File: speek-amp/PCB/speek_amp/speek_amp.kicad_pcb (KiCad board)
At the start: 2 copper layers, 70 parts, among them J1 Conn_01x02, J2 R_Tweeter, J3 R_Woofer, J5 L_Tweeter, J6 L_Sub, J7 L_Woofer, U1 TPA3116D2DAD_C2865736, U2 10uH, U3 10uH, U4 XT60, U5 10uH, U6 10uH, U7 PDMTAT068125-151MLU, U8 PDMTAT068125-151MLU

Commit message: a
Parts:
- added U9: 25PX4700MEFC16X25, easyeda2kicad:CAP-TH_BD16.0-P7.50-D1.2-FD, F.Cu at (22.1, 84.3)
- moved C1 143.4 mm to (45.7, 21.7)
- moved C10 143.4 mm to (45.7, 30.3)
- moved C11 143.4 mm to (45.7, 32.5)
- moved C12 143.4 mm to (45.7, 34.6)
- moved C21 143.4 mm to (51.5, 21.7)
- moved C22 143.4 mm to (51.5, 23.9)
- moved C23 143.4 mm to (51.5, 26.0)
- moved C24 143.4 mm to (51.5, 28.2)
- moved C25 143.4 mm to (51.5, 30.3)
- moved C26 143.4 mm to (51.5, 32.5)
- moved C27 143.4 mm to (51.5, 34.6)
- moved C6 143.4 mm to (45.7, 23.9)
- moved C7 143.4 mm to (45.7, 26.0)
- moved C8 143.4 mm to (45.7, 28.2)
- moved J1 143.4 mm to (59.2, 25.4)
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
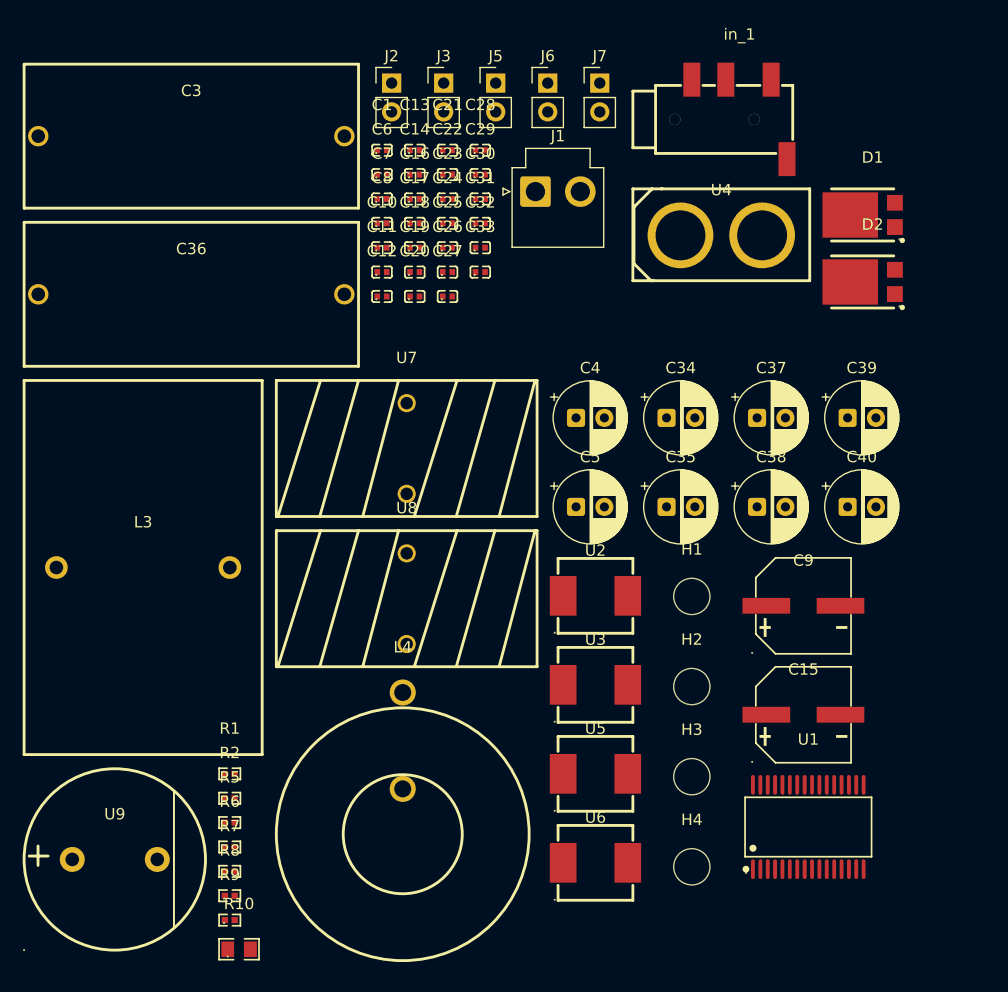
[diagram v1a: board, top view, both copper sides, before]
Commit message: [Speek Amp] Schematic rework
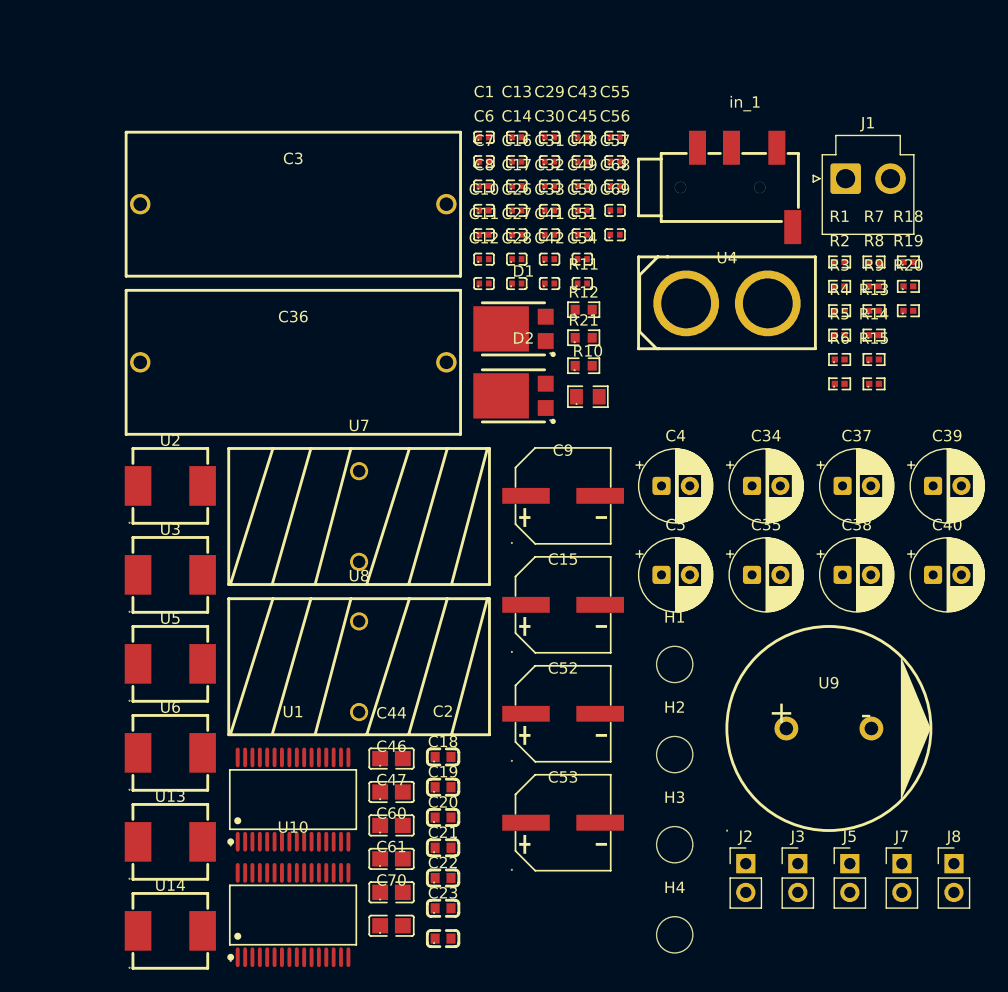
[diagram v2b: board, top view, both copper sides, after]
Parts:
- removed C24, C25: 100nF, easyeda2kicad:C0402
- removed J6: L_Sub, Connector_PinHeader_2.54mm:PinHeader_1x02_P2.54mm_Vertical
- removed L3: 1mH, easyeda2kicad:IND-TH_L33.0-W21.0-P15.3-D1.0
- removed L4: 220 uH, easyeda2kicad:IND-TH_BD22.3-P8.50-D1.2_XR068125TS221MHL8
- added C2: 100nF, easyeda2kicad:C0603, F.Cu at (51.1, 75.2)
- added C41: 1uF, easyeda2kicad:C0402, F.Cu at (60.5, 31.3)
- added C42: 1uF, easyeda2kicad:C0402, F.Cu at (60.5, 33.5)
- added C43: 100nF, easyeda2kicad:C0402, F.Cu at (63.4, 20.6)
- added C44: 680nF, easyeda2kicad:C0805, F.Cu at (46.5, 75.4)
- added C45: 1uF, easyeda2kicad:C0402, F.Cu at (63.4, 22.7)
- added C46: 680nF, easyeda2kicad:C0805, F.Cu at (46.5, 78.3)
- added C47: 680nF, easyeda2kicad:C0805, F.Cu at (46.5, 81.3)
- added C48: 220nF, easyeda2kicad:C0402, F.Cu at (63.4, 24.9)
- added C49: 220nF, easyeda2kicad:C0402, F.Cu at (63.4, 27.0)
- added C50: 220nF, easyeda2kicad:C0402, F.Cu at (63.4, 29.2)
- added C51: 220nF, easyeda2kicad:C0402, F.Cu at (63.4, 31.3)
- added C52: 220uF, easyeda2kicad:CAP-SMD_BD8.0-L8.3-W8.3-FD, F.Cu at (61.7, 71.4)
- added C53: 220uF, easyeda2kicad:CAP-SMD_BD8.0-L8.3-W8.3-FD, F.Cu at (61.7, 81.0)
- added C54: 100nF, easyeda2kicad:C0402, F.Cu at (63.4, 33.5)
- added C55: 100nF, easyeda2kicad:C0402, F.Cu at (66.3, 20.6)
- added C56: 1nF, easyeda2kicad:C0402, F.Cu at (66.3, 22.7)
- added C57: 1nF, easyeda2kicad:C0402, F.Cu at (66.3, 24.9)
- added C60: 680nF, easyeda2kicad:C0805, F.Cu at (46.5, 84.2)
- added C61: 680nF, easyeda2kicad:C0805, F.Cu at (46.5, 87.2)
- added C68: 1nF, easyeda2kicad:C0402, F.Cu at (66.3, 27.0)
- added C69: 1nF, easyeda2kicad:C0402, F.Cu at (66.3, 29.2)
- added C70: 680nF, easyeda2kicad:C0805, F.Cu at (46.5, 90.1)
- added J8: L_Sub, Connector_PinHeader_2.54mm:PinHeader_1x02_P2.54mm_Vertical, F.Cu at (96.1, 84.6)
- added R11: 3.2k, easyeda2kicad:R0603, F.Cu at (63.5, 35.8)
- added R12: 47k, easyeda2kicad:R0603, F.Cu at (63.5, 38.3)
- added R13: 3.3, easyeda2kicad:R0402, F.Cu at (89.1, 38.0)
- added R14: 100k, easyeda2kicad:R0402, F.Cu at (89.1, 40.2)
- added R15: 100k, easyeda2kicad:R0402, F.Cu at (89.1, 42.3)
- added R18: 3.3, easyeda2kicad:R0402, F.Cu at (92.1, 31.6)
- added R19: 3.3, easyeda2kicad:R0402, F.Cu at (92.1, 33.7)
- added R20: 10k, easyeda2kicad:R0402, F.Cu at (92.1, 35.9)
- added R21: 75k, easyeda2kicad:R0603, F.Cu at (63.5, 40.7)
- added R3: 10k, easyeda2kicad:R0402, F.Cu at (86.1, 35.9)
- added R4: 10k, easyeda2kicad:R0402, F.Cu at (86.1, 38.0)
- added U10: TPA3116D2DAD_C2865736, easyeda2kicad:HTSSOP-32_L11.0-W6.1-P0.65-LS8.1-BL, F.Cu at (37.9, 89.2)
- added U13: 10uH, easyeda2kicad:IND-SMD_L7.2-W6.6_GPSR07X0, F.Cu at (27.0, 82.7)
- added U14: 10uH, easyeda2kicad:IND-SMD_L7.2-W6.6_GPSR07X0, F.Cu at (27.0, 90.6)
- C18, C19, C20, C21: value 1uF -> 10nF; footprint easyeda2kicad:C0402 -> easyeda2kicad:C0603
- C22, C23: value 100nF -> 10nF; footprint easyeda2kicad:C0402 -> easyeda2kicad:C0603
- U9: value 25PX4700MEFC16X25 -> 50PX4700MEFC18X40; footprint easyeda2kicad:CAP-TH_BD16.0-P7.50-D1.2-FD -> easyeda2kicad:CAP-TH_BD18.0-P7.50-D0.8-FD
- moved R7 78.2 mm to (89.1, 31.6)
- moved R8 78.2 mm to (89.1, 33.7)
- moved R9 78.2 mm to (89.1, 35.9)
- moved J2 75.6 mm to (77.8, 84.6)
- moved J3 75.6 mm to (82.4, 84.6)
- moved J5 75.6 mm to (87.0, 84.6)
- moved J7 73.8 mm to (91.6, 84.6)
- moved R2 70.2 mm to (86.1, 33.7)
- moved R1 70.2 mm to (86.1, 31.6)
- moved R5 67.6 mm to (86.1, 40.2)
- moved R6 67.6 mm to (86.1, 42.3)
- moved C23 65.2 mm to (51.1, 91.3)
- moved C22 64.7 mm to (51.1, 88.6)
- moved C21 64.2 mm to (51.1, 85.9)
- moved U9 64.0 mm to (85.1, 72.7)
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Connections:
- C19 pad 1: /AMP_NR -> GND
- C19 pad 2: GND -> /AMP_NR
- C20 pad 1: /AMP_PL -> GND
- C20 pad 2: GND -> /AMP_PL
- C21 pad 1: /AMP_NL -> GND
- C21 pad 2: GND -> /AMP_NL
- C22 pad 1: /AMP_PR -> /SUB_P
- C23 pad 2: /AMP_NR -> /SUB_N
- U9 pad 1: /VCC -> /_VOUT

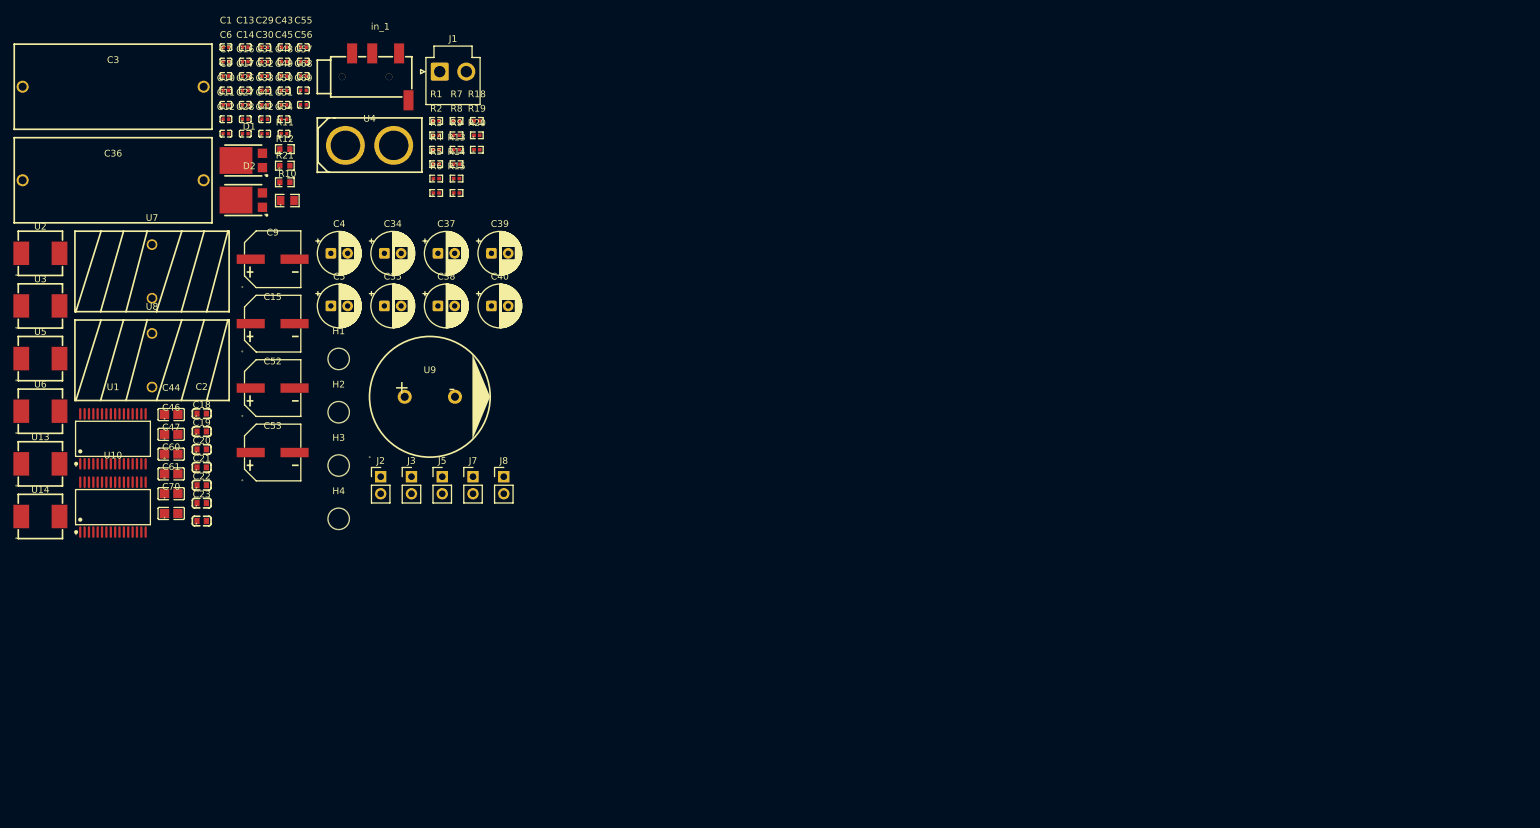
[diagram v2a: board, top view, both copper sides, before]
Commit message: [Speek amp] Prelim placement!!! [0.62 hours]
Long bom, many caps to place...
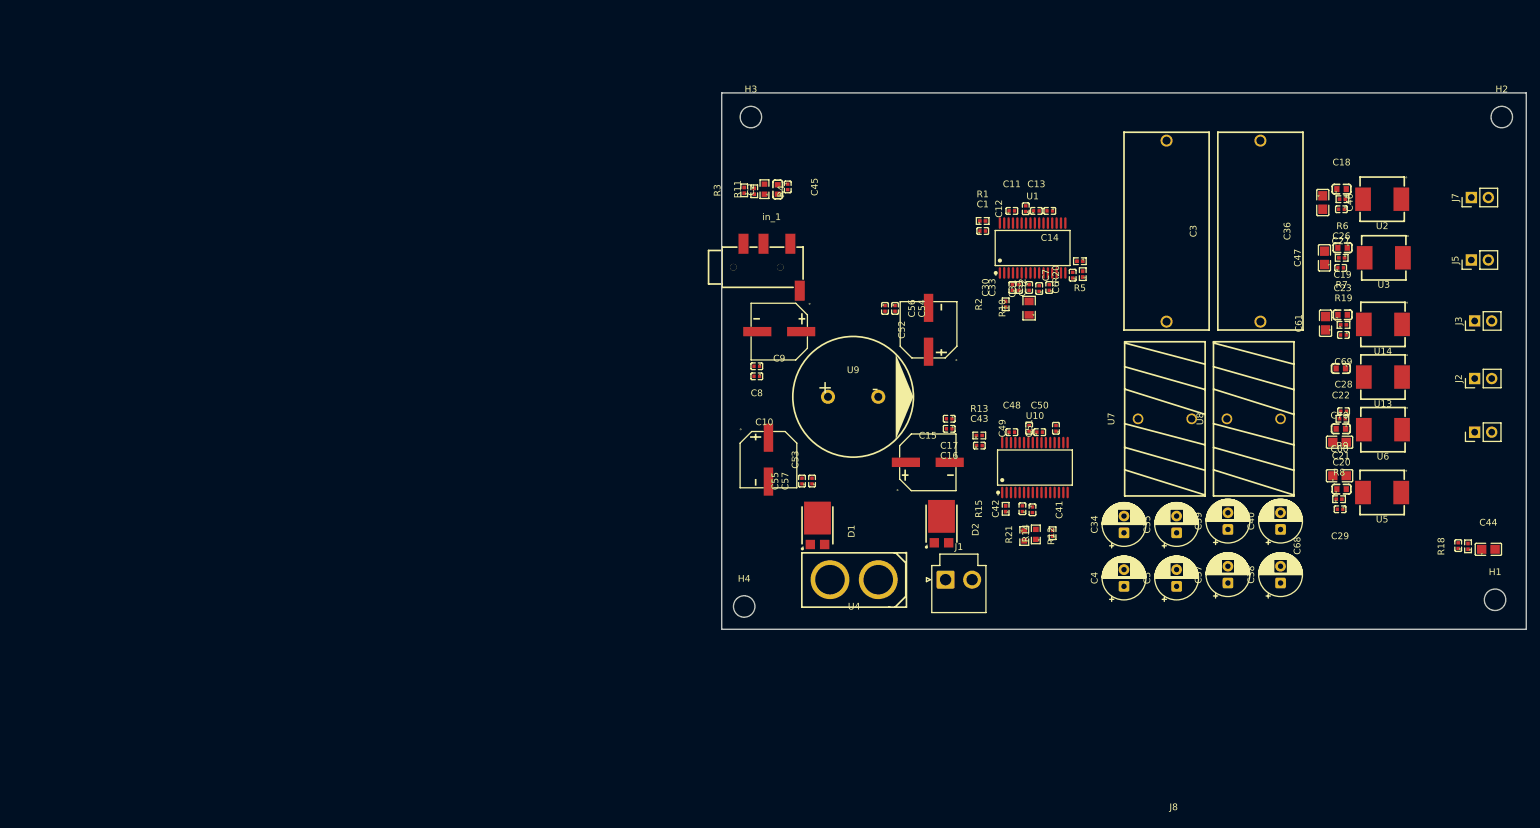
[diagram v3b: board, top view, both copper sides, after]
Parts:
- moved U14 202.3 mm to (227.3, 61.9), turned to 180 degrees
- moved U5 201.1 mm to (227.2, 87.0), turned to 180 degrees
- moved U13 200.7 mm to (227.3, 69.8), turned to 180 degrees
- moved U3 200.5 mm to (227.4, 52.0), turned to 180 degrees
- moved U2 200.3 mm to (227.2, 43.2), turned to 180 degrees
- moved U6 200.3 mm to (227.3, 77.6), turned to 180 degrees
- moved C44 197.5 mm to (243.0, 95.5)
- moved C68 185.1 mm to (238.5, 94.9), turned to 90 degrees
- moved H2 179.0 mm to (245.0, 31.0)
- moved H1 176.2 mm to (244.0, 103.0)
- moved C46 175.2 mm to (218.3, 43.8), turned to -90 degrees
- moved C70 174.6 mm to (220.8, 79.5)
- moved C29 174.6 mm to (220.9, 89.5), turned to 180 degrees
- moved C47 174.5 mm to (218.6, 52.0), turned to 90 degrees
- moved C60 174.3 mm to (220.8, 84.5)
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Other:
- board outline added: 120 x 80 mm

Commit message: [Speek Amp] routing !! [1.25 hours]
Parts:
- moved C38 73.7 mm to (239.0, 31.9), turned to 180 degrees
- moved C29 73.5 mm to (175.0, 32.1), turned to 90 degrees
- moved R8 71.4 mm to (176.5, 31.9), turned to -90 degrees
- moved C37 71.0 mm to (223.0, 32.0), turned to 180 degrees
- moved C20 69.2 mm to (178.0, 32.3), turned to -90 degrees
- moved U5 68.3 mm to (179.0, 38.5), turned to 90 degrees
- moved C60 66.5 mm to (180.0, 32.0), turned to -90 degrees
- moved C40 63.5 mm to (231.0, 31.9), turned to 180 degrees
- moved C39 62.3 mm to (236.0, 39.0), turned to 180 degrees
- moved U2 61.2 mm to (166.2, 37.8), turned to 90 degrees
- moved R6 53.4 mm to (169.0, 32.1), turned to -90 degrees
- moved C26 52.1 mm to (170.5, 32.2), turned to -90 degrees
- moved C46 51.1 mm to (169.2, 29.5), turned to 180 degrees
- moved C18 50.0 mm to (172.0, 32.3), turned to -90 degrees
- moved C4 46.9 mm to (233.5, 87.3), turned to 180 degrees
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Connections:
- U9 pad 1: /_VOUT -> /VCC
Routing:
- net /VCC: track 0.00 -> 233.7 mm
- net /OUTNR: track 0.00 -> 105.8 mm
- net /_OUTP: track 0.00 -> 97.1 mm, vias 0 -> 15
- net /_OUTN: track 0.00 -> 87.1 mm
- net /AMP_PR: track 0.00 -> 85.5 mm
- net /AMP_PL: track 0.00 -> 85.4 mm, vias 0 -> 6
- net /INL: track 0.00 -> 71.5 mm, vias 0 -> 2
- net Net-(U10-RINP): track 0.00 -> 71.4 mm, vias 0 -> 2
- net /INR: track 0.00 -> 65.1 mm, vias 0 -> 2
- net /OUTNL: track 0.00 -> 63.0 mm
- net Net-(C34-Pad1): track 0.00 -> 62.6 mm
- net GND: track 0.00 -> 60.9 mm, vias 0 -> 38
- net Net-(J3-Pin_1): track 0.00 -> 56.5 mm
- net /SYNC: track 0.00 -> 50.2 mm, vias 0 -> 2
- net Net-(J2-Pin_1): track 0.00 -> 49.5 mm
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- added copper zone on B.Cu, net GND
- added copper zone on F.Cu, net GND

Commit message: e
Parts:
- removed J1: Conn_01x02, Connector_JST:JST_VH_B2P-VH-B_1x02_P3.96mm_Vertical
- removed J2: R_Tweeter, Connector_PinHeader_2.54mm:PinHeader_1x02_P2.54mm_Vertical
- removed J3: R_Woofer, Connector_PinHeader_2.54mm:PinHeader_1x02_P2.54mm_Vertical
- removed J5: L_Tweeter, Connector_PinHeader_2.54mm:PinHeader_1x02_P2.54mm_Vertical
- removed J7: L_Woofer, Connector_PinHeader_2.54mm:PinHeader_1x02_P2.54mm_Vertical
- removed J8: L_Sub, Connector_PinHeader_2.54mm:PinHeader_1x02_P2.54mm_Vertical
- added U11: R_Tweeter, easyeda2kicad:CONN-TH_DB301V-3.5-2P-GN, F.Cu at (244.5, 70.0)
- added U12: R_Woofer, easyeda2kicad:CONN-TH_DB301V-3.5-2P-GN, F.Cu at (244.5, 60.5)
- added U15: L_Tweeter, easyeda2kicad:CONN-TH_DB301V-3.5-2P-GN, F.Cu at (244.5, 51.0)
- added U16: L_Woofer, easyeda2kicad:CONN-TH_DB301V-3.5-2P-GN, F.Cu at (244.5, 41.5)
- added U17: L_Sub, easyeda2kicad:CONN-TH_DB301V-3.5-2P-GN, F.Cu at (244.5, 79.8)
- added U18: J1, easyeda2kicad:CONN-TH_DB301V-3.5-2P-GN, F.Cu at (164.2, 100.1)
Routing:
- net Net-(C37-Pad2): track 35.4 -> 49.3 mm
- net Net-(C36-Pad2): track 37.0 -> 42.0 mm
- net /OUTNR: track 105.8 -> 110.8 mm
- net Net-(C3-Pad2): track 49.5 -> 53.7 mm
- net /AMP_NL: track 38.6 -> 42.6 mm
- net /SUB_P: track 29.9 -> 32.8 mm
- net /AMP_NR: track 41.9 -> 44.7 mm
- net Net-(C34-Pad2): track 56.5 -> 54.5 mm
- net /VCC: track 233.7 -> 233.2 mm

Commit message: vias
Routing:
- net GND: vias 38 -> 268

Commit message: yes!
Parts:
- moved H4 1.41 mm to (133.0, 103.0)
- moved C38 1.00 mm to (238.0, 32.0)
- moved H2 1.00 mm to (244.0, 31.0)
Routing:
- net Net-(C37-Pad2): track 49.3 -> 46.2 mm
- net Net-(C37-Pad1): track 41.7 -> 41.1 mm
- net (no net): vias 0 -> 1
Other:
- board text added: "Speek Amp"
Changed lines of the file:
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@@
 			(layer "F.Mask"
 				(type "Top Solder Mask")
+				(color "Black")
 				(thickness 0.01)
 			)
@@
 			(layer "B.Mask"
 				(type "Bottom Solder Mask")
+				(color "Black")
 				(thickness 0.01)
 			)
@@
 		(capping no)
 		(filling no)
+		(zone_defaults)
 		(pcbplotparams
 			(layerselection 0x00000000_00000000_55555555_5755f5ff)
@@
 	(footprint "Capacitor_THT:CP_Radial_D6.3mm_P2.50mm"
 		(layer "F.Cu")
-		(at 239 31.9 180)
+		(at 238 32 180)
 		(descr "CP, Radial series, Radial, pin pitch=2.50mm, diameter=6.3mm, height=7mm, Electrolytic Capacitor")
 		(tags "CP Radial series Radial pin pitch 2.50mm diameter 6.3mm height 7mm Electrolytic Capacitor")
@@
 	(footprint "MountingHole:MountingHole_3.2mm_M3"
 		(layer "F.Cu")
-		(at 245 31)
+		(at 244 31)
 		(descr "Mounting Hole 3.2mm, M3, no annular, generated by kicad-footprint-generator mountinghole.py")
 		(tags "mountinghole M3")
@@
 	(footprint "MountingHole:MountingHole_3.2mm_M3"
 		(layer "F.Cu")
-		(at 132 104)
+		(at 133 103)
 		(descr "Mounting Hole 3.2mm, M3, no annular, generated by kicad-footprint-generator mountinghole.py")
 		(tags "mountinghole M3")
@@
 		(layer "Edge.Cuts")
 	)
+	(gr_text "Speek Amp"
+		(at 182 101 0)
+		(layer "F.SilkS")
+		(effects
+			(font
+				(size 6 6)
+				(thickness 1)
+				(bold yes)
+			)
+			(justify left bottom)
+		)
+	)
+	(via
+		(at 94 52)
+		(size 0.6)
+		(drill 0.3)
+		(layers "F.Cu" "B.Cu")
+		(net "")
+	)
 	(segment
 		(start 219.675 43.75)
@@
 	)
 	(segment
-		(start 239 36)
-		(end 236 39)
+		(start 238 32)
+		(end 236.4 30.4)
 		(width 1)
 		(layer "B.Cu")
@@
 	)
 	(segment
+		(start 238 32)
+		(end 239 33)
+		(width 1)
+		(layer "B.Cu")
+		(net "Net-(C37-Pad1)")
+	)
+	(segment
 		(start 224.4 33.4)
 		(end 223.6 33.4)
@@
 	)
 	(segment
-		(start 232.514759 30.4)
-		(end 237.5 30.4)
+		(start 223.6 33.4)
+		(end 215 42)
 		(width 1)
 		(layer "B.Cu")
@@
 	)
 	(segment
-		(start 223.6 33.4)
-		(end 215 42)
+		(start 239 33)
+		(end 239 36)
 		(width 1)
 		(layer "B.Cu")
@@
 	)
 	(segment
-		(start 215 42)
-		(end 215 44)
+		(start 232.514759 30.4)
+		(end 236.4 30.4)
 		(width 1)
 		(layer "B.Cu")
@@
 	)
 	(segment
-		(start 239 31.9)
-		(end 239 36)
+		(start 239 36)
+		(end 236 39)
 		(width 1)
 		(layer "B.Cu")
@@
 	)
 	(segment
-		(start 237.5 30.4)
-		(end 239 31.9)
+		(start 215 42)
+		(end 215 44)
 		(width 1)
 		(layer "B.Cu")
@@
 	)
 	(segment
-		(start 230.014759 30.4)
-		(end 235 30.4)
+		(start 228.514759 31.9)
+		(end 230.014759 30.4)
 		(width 1)
 		(layer "F.Cu")
@@
 	)
 	(segment
-		(start 228.514759 31.9)
-		(end 230.014759 30.4)
+		(start 233.9 30.4)
+		(end 235.5 32)
 		(width 1)
 		(layer "F.Cu")
@@
 	)
 	(segment
-		(start 235 30.4)
-		(end 236.5 31.9)
+		(start 230.014759 30.4)
+		(end 233.9 30.4)
 		(width 1)
 		(layer "F.Cu")
@@
 	)
 	(segment
-		(start 233.5 39)
-		(end 237.5 43)
+		(start 235.5 32)
+		(end 236.5 33)
 		(width 1)
 		(layer "B.Cu")
@@
 	)
 	(segment
-		(start 236.5 31.9)
-		(end 236.5 36)
+		(start 241.086253 41)
+		(end 235.5 41)
 		(width 1)
 		(layer "B.Cu")
@@
 	)
 	(segment
-		(start 237.5 43)
-		(end 240.46 43)
+		(start 236.5 33)
+		(end 236.5 36)
 		(width 1)
 		(layer "B.Cu")
@@
 	)
 	(segment
-		(start 246.5 39.586253)
-		(end 246.5 41.25)
+		(start 233.5 39)
+		(end 235.5 41)
 		(width 1)
 		(layer "B.Cu")
@@
 	)
 	(segment
-		(start 246.5 41.25)
-		(end 244.5 43.25)
+		(start 246.5 39.586253)
+		(end 246.5 41.25)
 		(width 1)
 		(layer "B.Cu")
@@
 	)
 	(segment
-		(start 245.133747 38.22)
-		(end 246.5 39.586253)
+		(start 246.5 41.25)
+		(end 244.5 43.25)
 		(width 1)
 		(layer "B.Cu")
@@
 	)
 	(segment
-		(start 240.46 43)
-		(end 240.46 41.626253)
+		(start 236.5 36)
+		(end 233.5 39)
 		(width 1)
 		(layer "B.Cu")
@@
 	)
 	(segment
-		(start 222 30.5)
-		(end 220.5 32)
+		(start 243.866253 38.22)
+		(end 241.086253 41)
 		(width 1)
 		(layer "B.Cu")
@@
 	)
 	(segment
-		(start 236.5 36)
-		(end 233.5 39)
+		(start 245.133747 38.22)
+		(end 246.5 39.586253)
 		(width 1)
 		(layer "B.Cu")
@@
 	)
 	(segment
-		(start 240.46 41.626253)
-		(end 243.866253 38.22)
+		(start 222 30.5)
+		(end 220.5 32)
 		(width 1)
 		(layer "B.Cu")
